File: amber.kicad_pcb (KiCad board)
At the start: 2 copper layers, 118.9 x 112.3 mm, 51 parts, among them J1 SJ-43504-SMT-TR

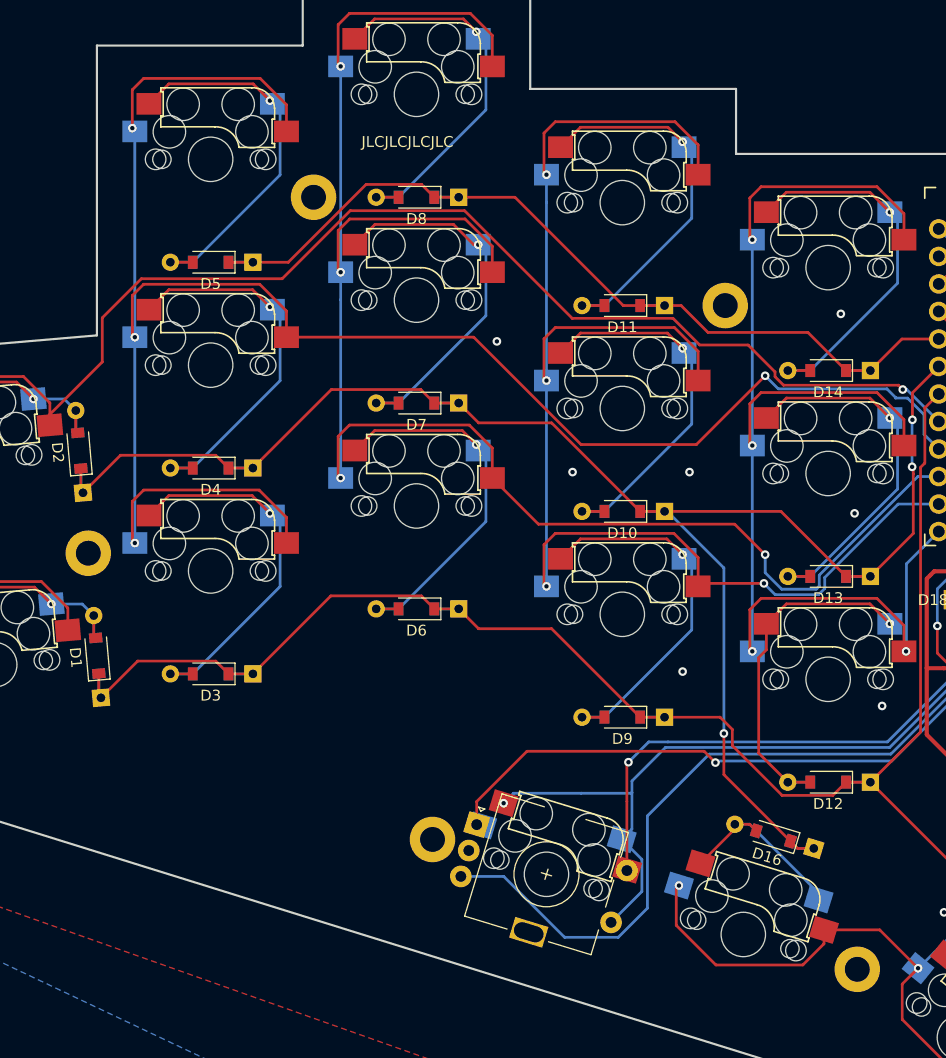
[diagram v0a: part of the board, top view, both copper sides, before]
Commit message: Let standoffs go through the PCB
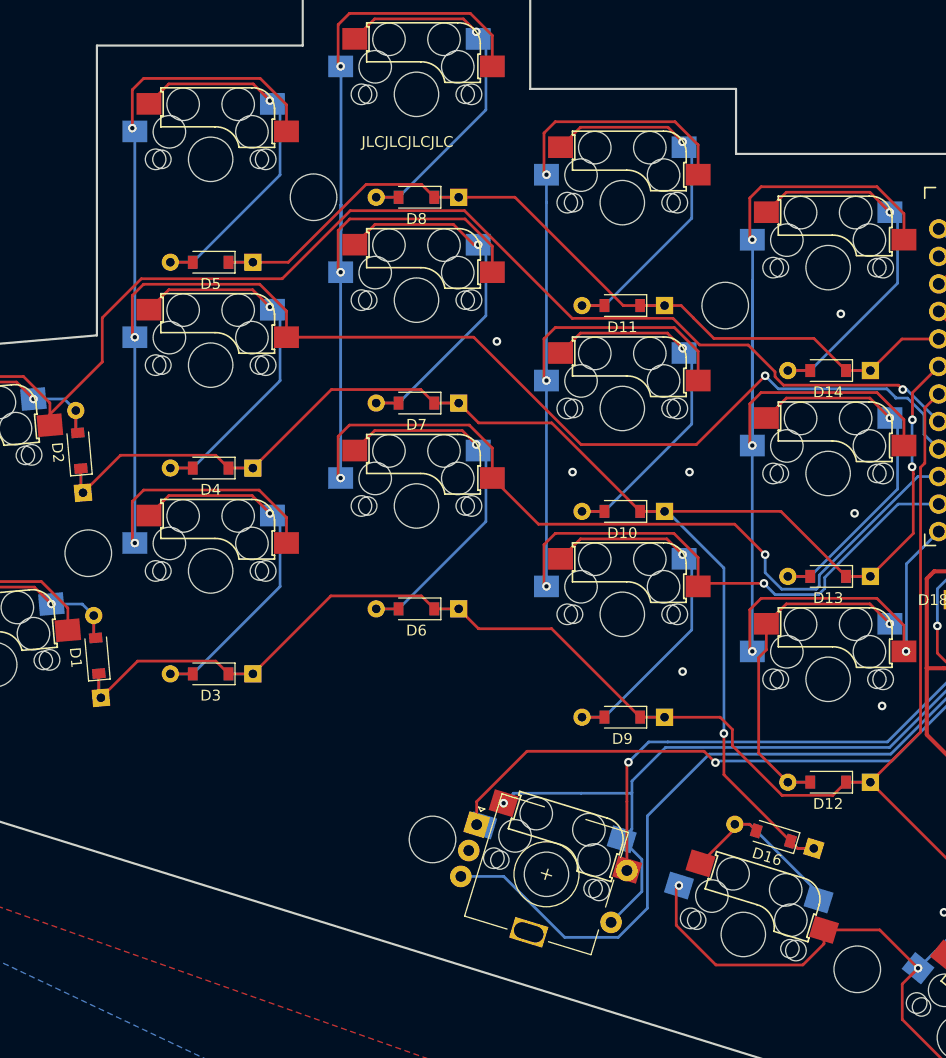
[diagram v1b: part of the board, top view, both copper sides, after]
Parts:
- P1, P2, P3, P4, P5: footprint kbd:M2_Hole_TH -> kbd:M2_HOLE_v2
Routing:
- net CN: track 116.4 -> 131.7 mm
- net CM: track 155.9 -> 162.2 mm

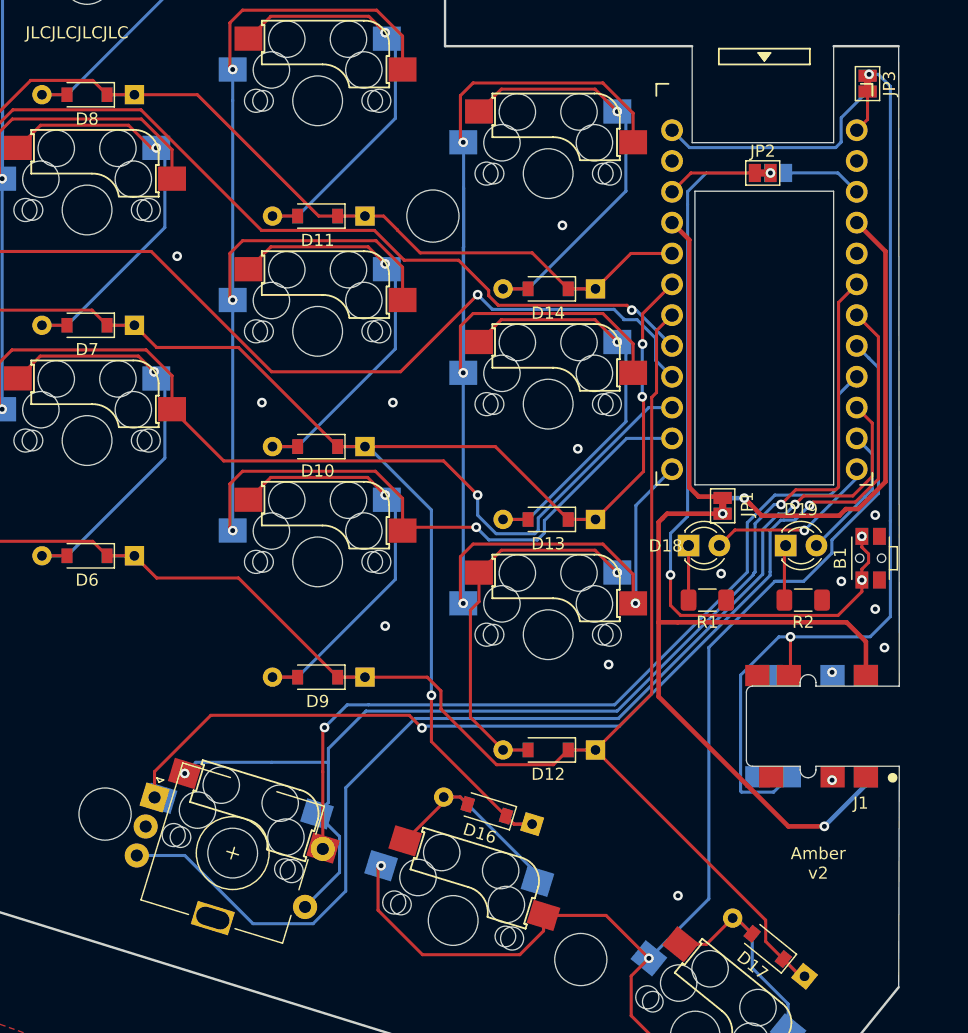
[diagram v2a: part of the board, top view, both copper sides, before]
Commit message: Replace 2 LEDs with one 5mm
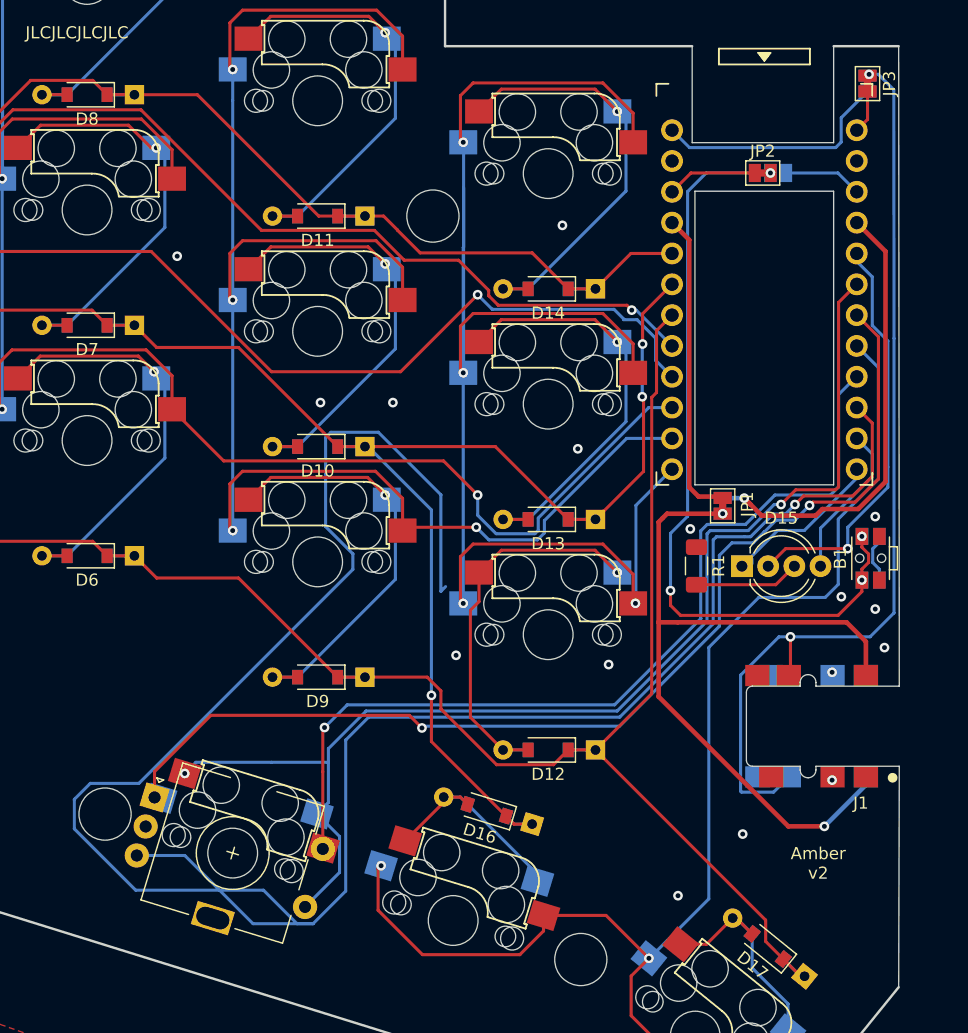
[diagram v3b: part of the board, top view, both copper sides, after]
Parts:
- removed D18, D19: LED, LED_THT:LED_D3.0mm
- removed R2: R, Resistor_SMD:R_1206_3216Metric_Pad1.30x1.75mm_HandSolder
- added D15: LED_BRCG, LED_THT:LED_D5.0mm-4_RGB_Wide_Pins, F.Cu at (92.9, -4.30)
- moved R1 2.96 mm to (89.2, -4.32), turned to 270 degrees
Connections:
- C1 pad 5: Net-(C1-Pad5) -> LED3
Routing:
- net EB: track 91.6 -> 184.0 mm
- net LED3: track 0.00 -> 33.9 mm, vias 0 -> 1
- net Net-(D19-Pad1): track 4.54 -> 0.00 mm
- net Net-(D15-Pad3): track 4.50 -> 8.70 mm
- net GND: track 0.00 -> 4.06 mm, vias 15 -> 16
- net RE: track 72.5 -> 74.4 mm
- net CE: track 98.3 -> 100.1 mm
- net LED2: track 11.3 -> 12.8 mm
- net EA: track 89.0 -> 90.3 mm
- net CT: track 113.4 -> 114.6 mm
- net LED1: track 14.5 -> 13.6 mm, vias 1 -> 0

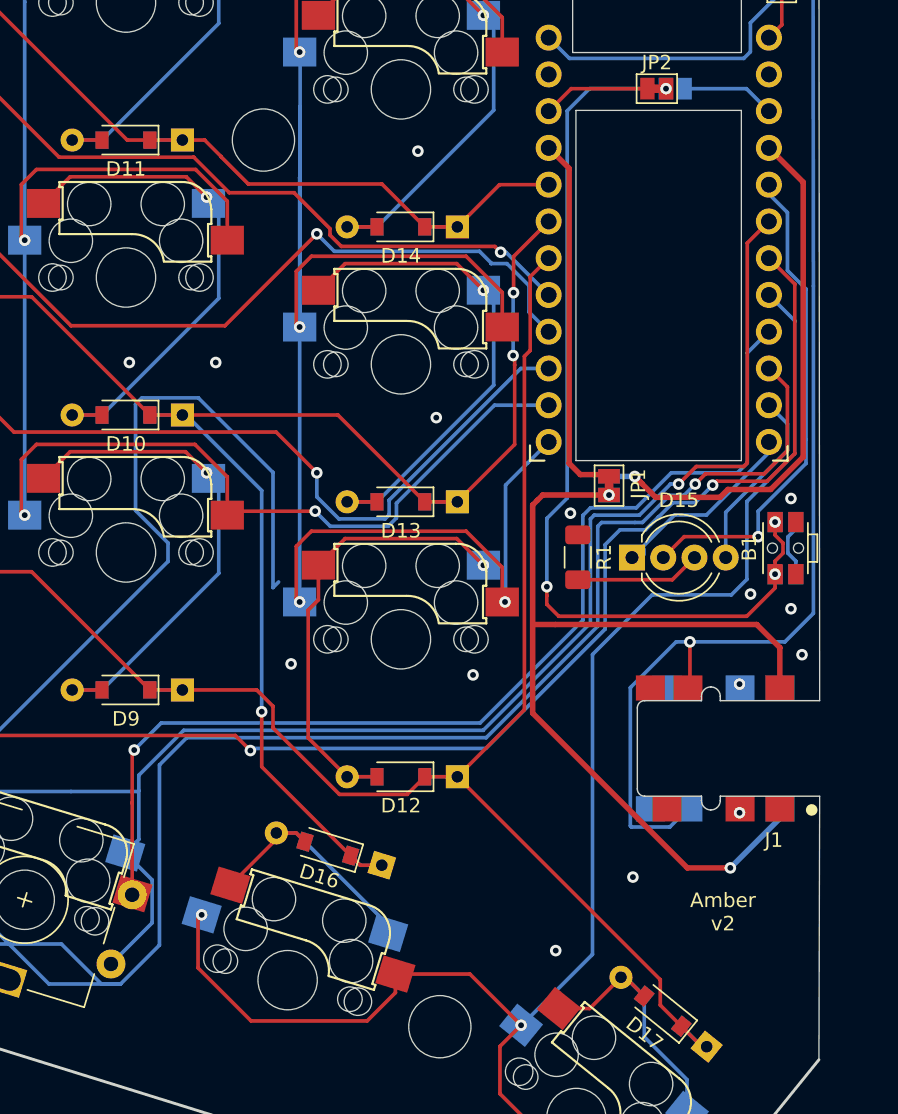
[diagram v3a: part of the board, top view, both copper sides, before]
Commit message: Add a pixel LED indicator option
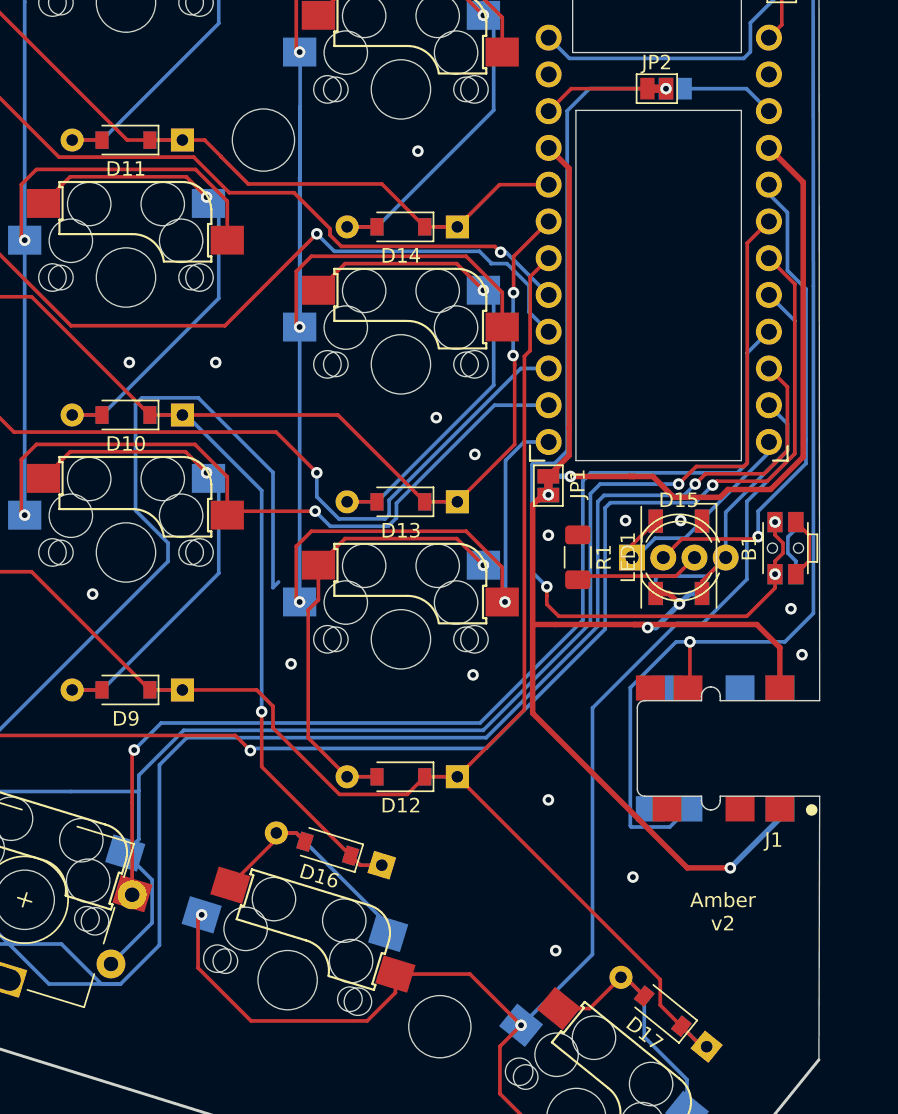
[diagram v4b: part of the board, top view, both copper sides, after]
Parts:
- added LED1: YS-SK6812MINI-E, amber:LED_WS2812B-PLCC4-dual, F.Cu at (96.1, -4.32)
- moved JP1 4.19 mm to (87.1, -9.27)
- moved JP6 4.19 mm to (87.1, -9.27)
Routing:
- net LED2: track 12.8 -> 22.5 mm
- net Net-(C1-Pad4): track 37.7 -> 42.1 mm
- net GND: track 4.06 -> 8.41 mm, vias 16 -> 17
- net VCC: track 66.4 -> 69.5 mm, vias 2 -> 4
- net LED1: track 13.6 -> 15.9 mm
- net CT: track 114.6 -> 112.4 mm
- net RST: track 64.1 -> 65.8 mm
- net Net-(C1-Pad21): track 25.5 -> 23.9 mm
- net EA: track 90.3 -> 91.8 mm
- net RE: track 74.4 -> 75.8 mm
- net CE: track 100.1 -> 101.2 mm
- net EB: track 184.0 -> 185.0 mm
- net CN: track 131.7 -> 132.7 mm

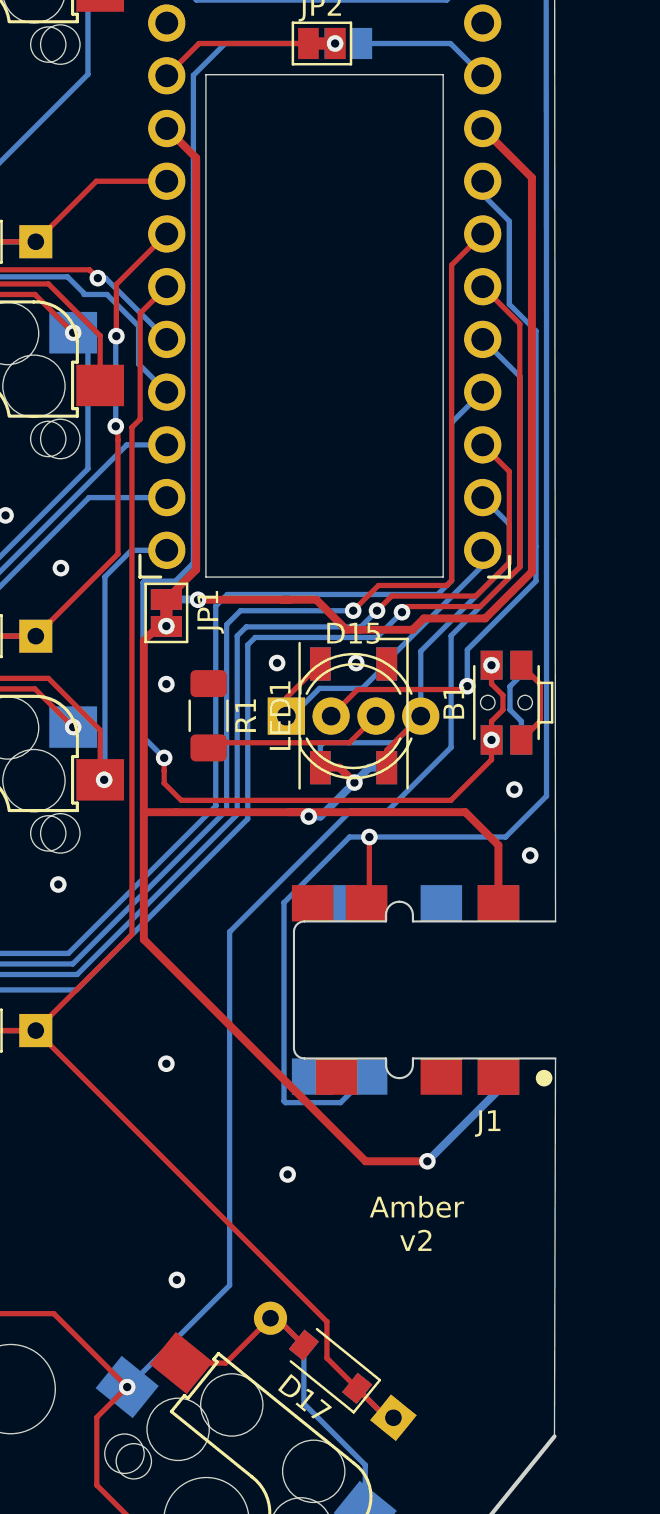
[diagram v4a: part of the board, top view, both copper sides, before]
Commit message: Make pixel LEDs easier to solder
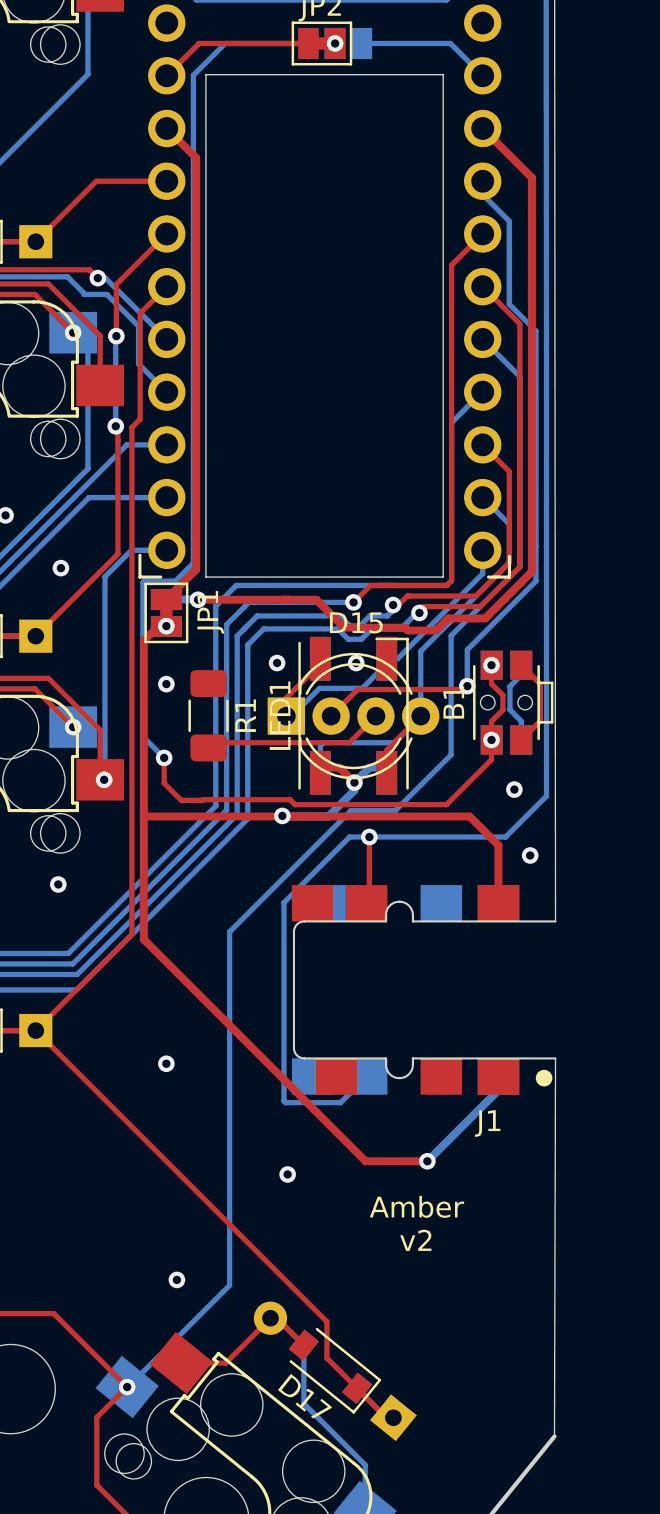
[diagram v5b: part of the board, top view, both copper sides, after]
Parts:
- D15: footprint LED_THT:LED_D5.0mm-4_RGB_Wide_Pins -> amber:LED_D5.0mm-4_RGB_Wide_Pins-dual
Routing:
- net VCC: track 69.5 -> 67.6 mm
- net CE: track 101.2 -> 101.9 mm
- net EB: track 185.0 -> 185.7 mm
- net LED1: track 15.9 -> 16.5 mm

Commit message: Cleanup tracks
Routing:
- net EB: track 185.7 -> 96.2 mm
- net RE: track 75.8 -> 74.4 mm
- net EA: track 92.2 -> 91.1 mm
- net CE: track 101.9 -> 100.9 mm
